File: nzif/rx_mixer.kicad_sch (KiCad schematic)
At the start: 24 parts, among them U107 SN74CBT355CPW, U108 SN74CBT355CPW, U112 SN74CBT355CPW, U113 SN74CBT355CPW, U5 ADA4625-2, U6 ADA4625-2, U7 ADA4625-2, U8 ADA4625-2

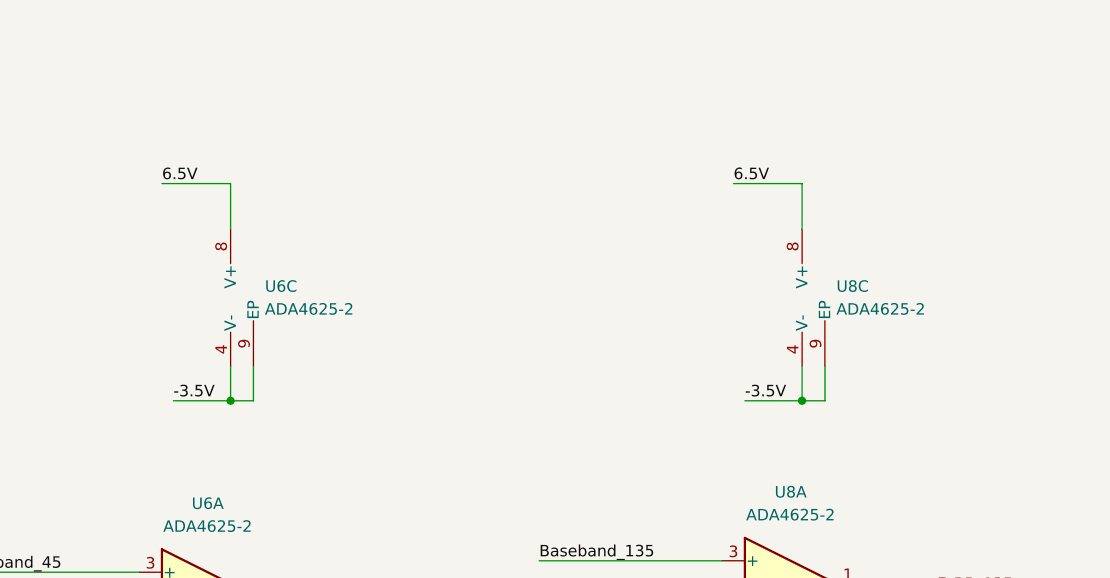
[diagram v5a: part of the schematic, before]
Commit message: update digikey parts for rx mixer
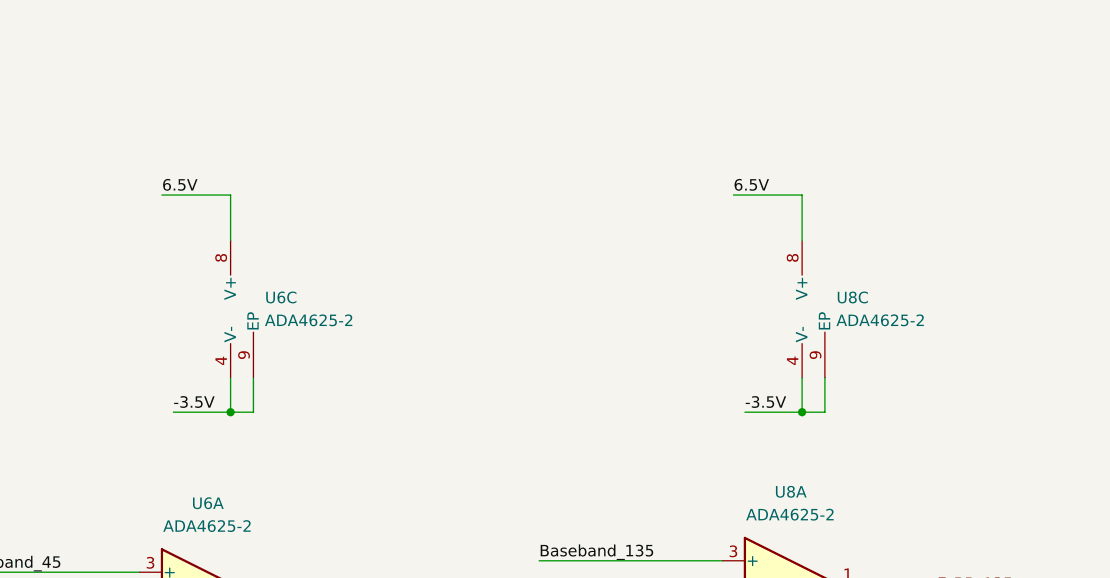
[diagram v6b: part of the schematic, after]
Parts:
- HC_101, HC_102, HC_103, HC_104, HC_105, HC_106, HC_107, HC_108: footprint Capacitor_SMD:C_0603_1608Metric_Pad1.08x0.95mm_HandSolder -> Capacitor_SMD:C_1206_3216Metric_Pad1.33x1.80mm_HandSolder
- U5, U6, U7, U8: Digikey Part # (none) -> 505-ADA4625-2ARDZ-R7CT-ND
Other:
- moved on the sheet: U6C, U8C
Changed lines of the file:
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@@
 	)
 	(junction
-		(at 187.96 208.28)
+		(at 187.96 209.55)
 		(diameter 0)
 		(color 0 0 0 0)
@@
 	)
 	(junction
-		(at 251.46 208.28)
+		(at 251.46 209.55)
 		(diameter 0)
 		(color 0 0 0 0)
@@
 	(wire
 		(pts
-			(xy 243.84 184.15) (xy 251.46 184.15)
+			(xy 243.84 185.42) (xy 251.46 185.42)
 		)
 		(stroke
@@
 	(wire
 		(pts
-			(xy 181.61 208.28) (xy 187.96 208.28)
+			(xy 181.61 209.55) (xy 187.96 209.55)
 		)
 		(stroke
@@
 	(wire
 		(pts
-			(xy 180.34 184.15) (xy 187.96 184.15)
+			(xy 180.34 185.42) (xy 187.96 185.42)
 		)
 		(stroke
@@
 	(wire
 		(pts
-			(xy 254 204.47) (xy 254 208.28)
+			(xy 254 205.74) (xy 254 209.55)
 		)
 		(stroke
@@
 	(wire
 		(pts
-			(xy 190.5 204.47) (xy 190.5 208.28)
+			(xy 190.5 205.74) (xy 190.5 209.55)
 		)
 		(stroke
@@
 	(wire
 		(pts
-			(xy 254 208.28) (xy 251.46 208.28)
+			(xy 254 209.55) (xy 251.46 209.55)
 		)
 		(stroke
@@
 	(wire
 		(pts
-			(xy 187.96 208.28) (xy 187.96 204.47)
+			(xy 187.96 209.55) (xy 187.96 205.74)
 		)
 		(stroke
@@
 	(wire
 		(pts
-			(xy 190.5 208.28) (xy 187.96 208.28)
+			(xy 190.5 209.55) (xy 187.96 209.55)
 		)
 		(stroke
@@
 	(wire
 		(pts
-			(xy 251.46 184.15) (xy 251.46 189.23)
+			(xy 251.46 185.42) (xy 251.46 190.5)
 		)
 		(stroke
@@
 	(wire
 		(pts
-			(xy 245.11 208.28) (xy 251.46 208.28)
+			(xy 245.11 209.55) (xy 251.46 209.55)
 		)
 		(stroke
@@
 	(wire
 		(pts
-			(xy 251.46 208.28) (xy 251.46 204.47)
+			(xy 251.46 209.55) (xy 251.46 205.74)
 		)
 		(stroke
@@
 	(wire
 		(pts
-			(xy 187.96 184.15) (xy 187.96 189.23)
+			(xy 187.96 185.42) (xy 187.96 190.5)
 		)
 		(stroke
@@
 	)
 	(label "-3.5V"
-		(at 181.61 208.28 0)
+		(at 181.61 209.55 0)
 		(effects
 			(font
@@
 	)
 	(label "6.5V"
-		(at 243.84 184.15 0)
+		(at 243.84 185.42 0)
 		(effects
 			(font
@@
 	)
 	(label "6.5V"
-		(at 180.34 184.15 0)
+		(at 180.34 185.42 0)
 		(effects
 			(font
@@
 	)
 	(label "-3.5V"
-		(at 245.11 208.28 0)
+		(at 245.11 209.55 0)
 		(effects
 			(font
@@
 			)
 		)
-		(property "Digikey Part #" ""
+		(property "Digikey Part #" "505-ADA4625-2ARDZ-R7CT-ND"
 			(at 120.65 251.46 0)
 			(effects
@@
 			)
 		)
-		(property "Digikey Part #" ""
+		(property "Digikey Part #" "505-ADA4625-2ARDZ-R7CT-ND"
 			(at 185.42 229.87 0)
 			(effects
@@
 	(symbol
 		(lib_id "Amplifier_Operational:ADA4625-2ARDZ")
-		(at 254 196.85 0)
+		(at 254 198.12 0)
 		(unit 3)
 		(exclude_from_sim no)
@@
 		(fields_autoplaced yes)
 		(property "Reference" "U?"
-			(at 255.27 195.5799 0)
+			(at 255.27 196.8499 0)
 			(effects
 				(font
@@
 		)
 		(property "Value" "ADA4625-2"
-			(at 255.27 198.1199 0)
+			(at 255.27 199.3899 0)
 			(effects
 				(font
@@
 		)
 		(property "Footprint" "Package_SO:SOIC-8-1EP_3.9x4.9mm_P1.27mm_EP2.29x3mm"
-			(at 252.73 204.47 0)
+			(at 252.73 205.74 0)
 			(effects
 				(font
@@
 		)
 		(property "Datasheet" "https://www.analog.com/media/en/technical-documentation/data-sheets/ADA4625-1-4625-2.pdf"
-			(at 254 196.85 0)
+			(at 254 198.12 0)
 			(effects
 				(font
@@
 		)
 		(property "Description" "Dual 5V..36V/±2.5V..±18V supply, 18 MHz, 48V/µs slew rate, ±80 µV offset, RRO, Fast-settling JFET Op Amp, SOIC-8-1EP"
-			(at 254 196.85 0)
+			(at 254 198.12 0)
 			(effects
 				(font
@@
 			)
 		)
-		(property "Digikey Part #" ""
-			(at 254 196.85 0)
+		(property "Digikey Part #" "505-ADA4625-2ARDZ-R7CT-ND"
+			(at 254 198.12 0)
 			(effects
 				(font
@@
 			)
 		)
-		(property "Digikey Part #" ""
+		(property "Digikey Part #" "505-ADA4625-2ARDZ-R7CT-ND"
 			(at 63.5 198.12 0)
 			(effects
@@
 			)
 		)
-		(property "Digikey Part #" ""
+		(property "Digikey Part #" "505-ADA4625-2ARDZ-R7CT-ND"
 			(at 60.96 248.92 0)
 			(effects
@@
 			)
 		)
-		(property "Digikey Part #" ""
+		(property "Digikey Part #" "505-ADA4625-2ARDZ-R7CT-ND"
 			(at 125.73 198.12 0)
 			(effects
@@
 			)
 		)
-		(property "Digikey Part #" ""
+		(property "Digikey Part #" "505-ADA4625-2ARDZ-R7CT-ND"
 			(at 250.19 248.92 0)
 			(effects
@@
 			)
 		)
-		(property "Footprint" "Capacitor_SMD:C_0603_1608Metric_Pad1.08x0.95mm_HandSolder"
+		(property "Footprint" "Capacitor_SMD:C_1206_3216Metric_Pad1.33x1.80mm_HandSolder"
 			(at 285.75 50.8 0)
 			(effects
@@
 			)
 		)
-		(property "Digikey Part #" ""
+		(property "Digikey Part #" "505-ADA4625-2ARDZ-R7CT-ND"
 			(at 185.42 250.19 0)
 			(effects
@@
 			)
 		)
-		(property "Digikey Part #" ""
+		(property "Digikey Part #" "505-ADA4625-2ARDZ-R7CT-ND"
 			(at 250.19 228.6 0)
 			(effects
@@
 			)
 		)
-		(property "Footprint" "Capacitor_SMD:C_0603_1608Metric_Pad1.08x0.95mm_HandSolder"
+		(property "Footprint" "Capacitor_SMD:C_1206_3216Metric_Pad1.33x1.80mm_HandSolder"
 			(at 171.45 138.43 0)
 			(effects
@@
 			)
 		)
-		(property "Footprint" "Capacitor_SMD:C_0603_1608Metric_Pad1.08x0.95mm_HandSolder"
+		(property "Footprint" "Capacitor_SMD:C_1206_3216Metric_Pad1.33x1.80mm_HandSolder"
 			(at 170.18 64.77 0)
 			(effects
@@
 			)
 		)
-		(property "Footprint" "Capacitor_SMD:C_0603_1608Metric_Pad1.08x0.95mm_HandSolder"
+		(property "Footprint" "Capacitor_SMD:C_1206_3216Metric_Pad1.33x1.80mm_HandSolder"
 			(at 171.45 123.19 0)
 			(effects
@@
 			)
 		)
-		(property "Footprint" "Capacitor_SMD:C_0603_1608Metric_Pad1.08x0.95mm_HandSolder"
+		(property "Footprint" "Capacitor_SMD:C_1206_3216Metric_Pad1.33x1.80mm_HandSolder"
 			(at 170.18 49.53 0)
 			(effects
@@
 	(symbol
 		(lib_id "Amplifier_Operational:ADA4625-2ARDZ")
-		(at 190.5 196.85 0)
+		(at 190.5 198.12 0)
 		(unit 3)
 		(exclude_from_sim no)
@@
 		(fields_autoplaced yes)
 		(property "Reference" "U?"
-			(at 191.77 195.5799 0)
+			(at 191.77 196.8499 0)
 			(effects
 				(font
@@
 		)
 		(property "Value" "ADA4625-2"
-			(at 191.77 198.1199 0)
+			(at 191.77 199.3899 0)
 			(effects
 				(font
@@
 		)
 		(property "Footprint" "Package_SO:SOIC-8-1EP_3.9x4.9mm_P1.27mm_EP2.29x3mm"
-			(at 189.23 204.47 0)
+			(at 189.23 205.74 0)
 			(effects
 				(font
@@
 		)
 		(property "Datasheet" "https://www.analog.com/media/en/technical-documentation/data-sheets/ADA4625-1-4625-2.pdf"
-			(at 190.5 196.85 0)
+			(at 190.5 198.12 0)
 			(effects
 				(font
@@
 		)
 		(property "Description" "Dual 5V..36V/±2.5V..±18V supply, 18 MHz, 48V/µs slew rate, ±80 µV offset, RRO, Fast-settling JFET Op Amp, SOIC-8-1EP"
-			(at 190.5 196.85 0)
+			(at 190.5 198.12 0)
 			(effects
 				(font
@@
 			)
 		)
-		(property "Digikey Part #" ""
-			(at 190.5 196.85 0)
+		(property "Digikey Part #" "505-ADA4625-2ARDZ-R7CT-ND"
+			(at 190.5 198.12 0)
 			(effects
 				(font
@@
 			)
 		)
-		(property "Footprint" "Capacitor_SMD:C_0603_1608Metric_Pad1.08x0.95mm_HandSolder"
+		(property "Footprint" "Capacitor_SMD:C_1206_3216Metric_Pad1.33x1.80mm_HandSolder"
 			(at 285.75 66.04 0)
 			(effects
@@
 			)
 		)
-		(property "Digikey Part #" ""
+		(property "Digikey Part #" "505-ADA4625-2ARDZ-R7CT-ND"
 			(at 121.92 231.14 0)
 			(effects
@@
 			)
 		)
-		(property "Digikey Part #" ""
+		(property "Digikey Part #" "505-ADA4625-2ARDZ-R7CT-ND"
 			(at 60.96 228.6 0)
 			(effects
@@
 			)
 		)
-		(property "Footprint" "Capacitor_SMD:C_0603_1608Metric_Pad1.08x0.95mm_HandSolder"
+		(property "Footprint" "Capacitor_SMD:C_1206_3216Metric_Pad1.33x1.80mm_HandSolder"
 			(at 287.02 139.7 0)
 			(effects
@@
 			)
 		)
-		(property "Footprint" "Capacitor_SMD:C_0603_1608Metric_Pad1.08x0.95mm_HandSolder"
+		(property "Footprint" "Capacitor_SMD:C_1206_3216Metric_Pad1.33x1.80mm_HandSolder"
 			(at 287.02 124.46 0)
 			(effects

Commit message: Digikey parts for rcv stages
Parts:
- HC_101, HC_102, HC_103, HC_104, HC_105, HC_106, HC_107, HC_108: Digikey Part # (none) -> 490-GCM31C5C1H104FA16LCT-ND
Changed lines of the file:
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@@
 			)
 		)
-		(property "Datasheet" "~"
+		(property "Datasheet" "https://search.murata.co.jp/Ceramy/image/img/A01X/G101/ENG/GCM31C5C1H104FA16-01.pdf"
 			(at 285.75 50.8 0)
 			(effects
@@
 			)
 		)
-		(property "Digikey Part #" ""
+		(property "Digikey Part #" "490-GCM31C5C1H104FA16LCT-ND"
 			(at 285.75 50.8 90)
 			(effects
@@
 			)
 		)
-		(property "Datasheet" "~"
+		(property "Datasheet" "https://search.murata.co.jp/Ceramy/image/img/A01X/G101/ENG/GCM31C5C1H104FA16-01.pdf"
 			(at 171.45 138.43 0)
 			(effects
@@
 			)
 		)
-		(property "Digikey Part #" ""
+		(property "Digikey Part #" "490-GCM31C5C1H104FA16LCT-ND"
 			(at 171.45 138.43 90)
 			(effects
@@
 			)
 		)
-		(property "Datasheet" "~"
+		(property "Datasheet" "https://search.murata.co.jp/Ceramy/image/img/A01X/G101/ENG/GCM31C5C1H104FA16-01.pdf"
 			(at 170.18 64.77 0)
 			(effects
@@
 			)
 		)
-		(property "Digikey Part #" ""
+		(property "Digikey Part #" "490-GCM31C5C1H104FA16LCT-ND"
 			(at 170.18 64.77 90)
 			(effects
@@
 			)
 		)
-		(property "Datasheet" "~"
+		(property "Datasheet" "https://search.murata.co.jp/Ceramy/image/img/A01X/G101/ENG/GCM31C5C1H104FA16-01.pdf"
 			(at 171.45 123.19 0)
 			(effects
@@
 			)
 		)
-		(property "Digikey Part #" ""
+		(property "Digikey Part #" "490-GCM31C5C1H104FA16LCT-ND"
 			(at 171.45 123.19 90)
 			(effects
@@
 			)
 		)
-		(property "Datasheet" "~"
+		(property "Datasheet" "https://search.murata.co.jp/Ceramy/image/img/A01X/G101/ENG/GCM31C5C1H104FA16-01.pdf"
 			(at 170.18 49.53 0)
 			(effects
@@
 			)
 		)
-		(property "Digikey Part #" ""
+		(property "Digikey Part #" "490-GCM31C5C1H104FA16LCT-ND"
 			(at 170.18 49.53 90)
 			(effects
@@
 			)
 		)
-		(property "Datasheet" "~"
+		(property "Datasheet" "https://search.murata.co.jp/Ceramy/image/img/A01X/G101/ENG/GCM31C5C1H104FA16-01.pdf"
 			(at 285.75 66.04 0)
 			(effects
@@
 			)
 		)
-		(property "Digikey Part #" ""
+		(property "Digikey Part #" "490-GCM31C5C1H104FA16LCT-ND"
 			(at 285.75 66.04 90)
 			(effects
@@
 			)
 		)
-		(property "Datasheet" "~"
+		(property "Datasheet" "https://search.murata.co.jp/Ceramy/image/img/A01X/G101/ENG/GCM31C5C1H104FA16-01.pdf"
 			(at 287.02 139.7 0)
 			(effects
@@
 			)
 		)
-		(property "Digikey Part #" ""
+		(property "Digikey Part #" "490-GCM31C5C1H104FA16LCT-ND"
 			(at 287.02 139.7 90)
 			(effects
@@
 			)
 		)
-		(property "Datasheet" "~"
+		(property "Datasheet" "https://search.murata.co.jp/Ceramy/image/img/A01X/G101/ENG/GCM31C5C1H104FA16-01.pdf"
 			(at 287.02 124.46 0)
 			(effects
@@
 			)
 		)
-		(property "Digikey Part #" ""
+		(property "Digikey Part #" "490-GCM31C5C1H104FA16LCT-ND"
 			(at 287.02 124.46 90)
 			(effects

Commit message: add annotations - first run of erc
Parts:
- renumbered U7 to U101, U5 to U102, U107 to U103, U108 to U104, U6 to U105, U112 to U106, U113 to U107, U8 to U108
